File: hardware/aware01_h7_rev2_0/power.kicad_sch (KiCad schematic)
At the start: 23 parts, among them J3 Conn_02x05_Odd_Even, U7 LM1117MP-3.3, U8 LM4040DIM3X-10

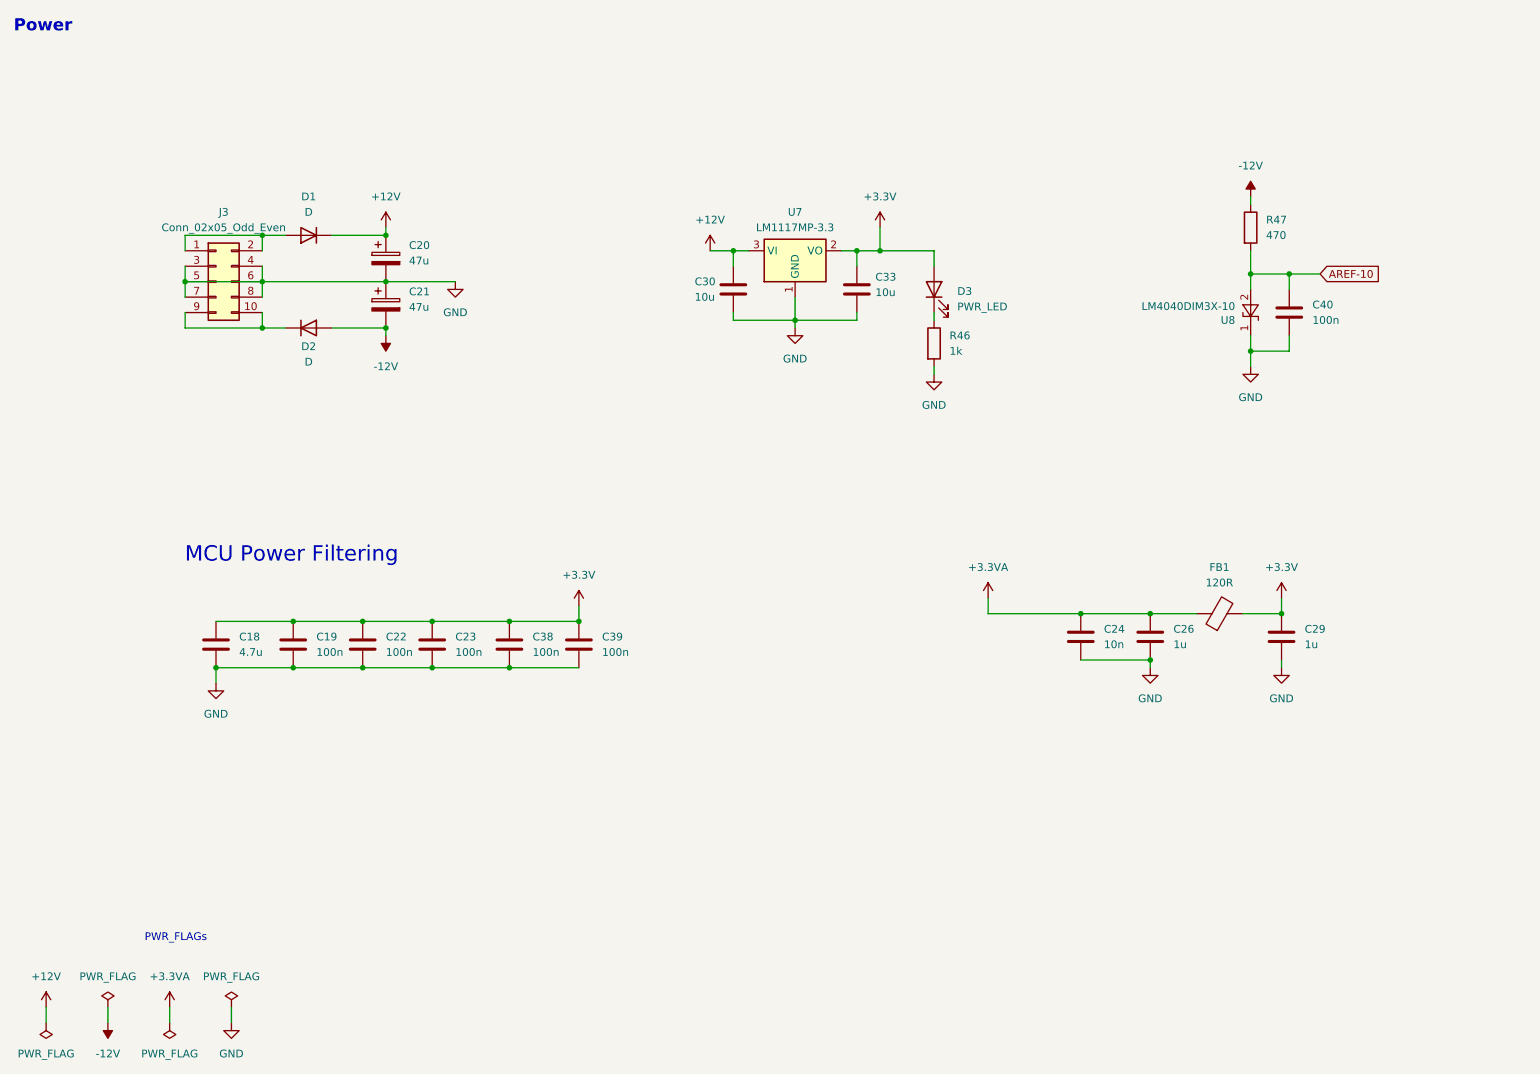
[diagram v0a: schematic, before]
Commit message: add 5V buck converter
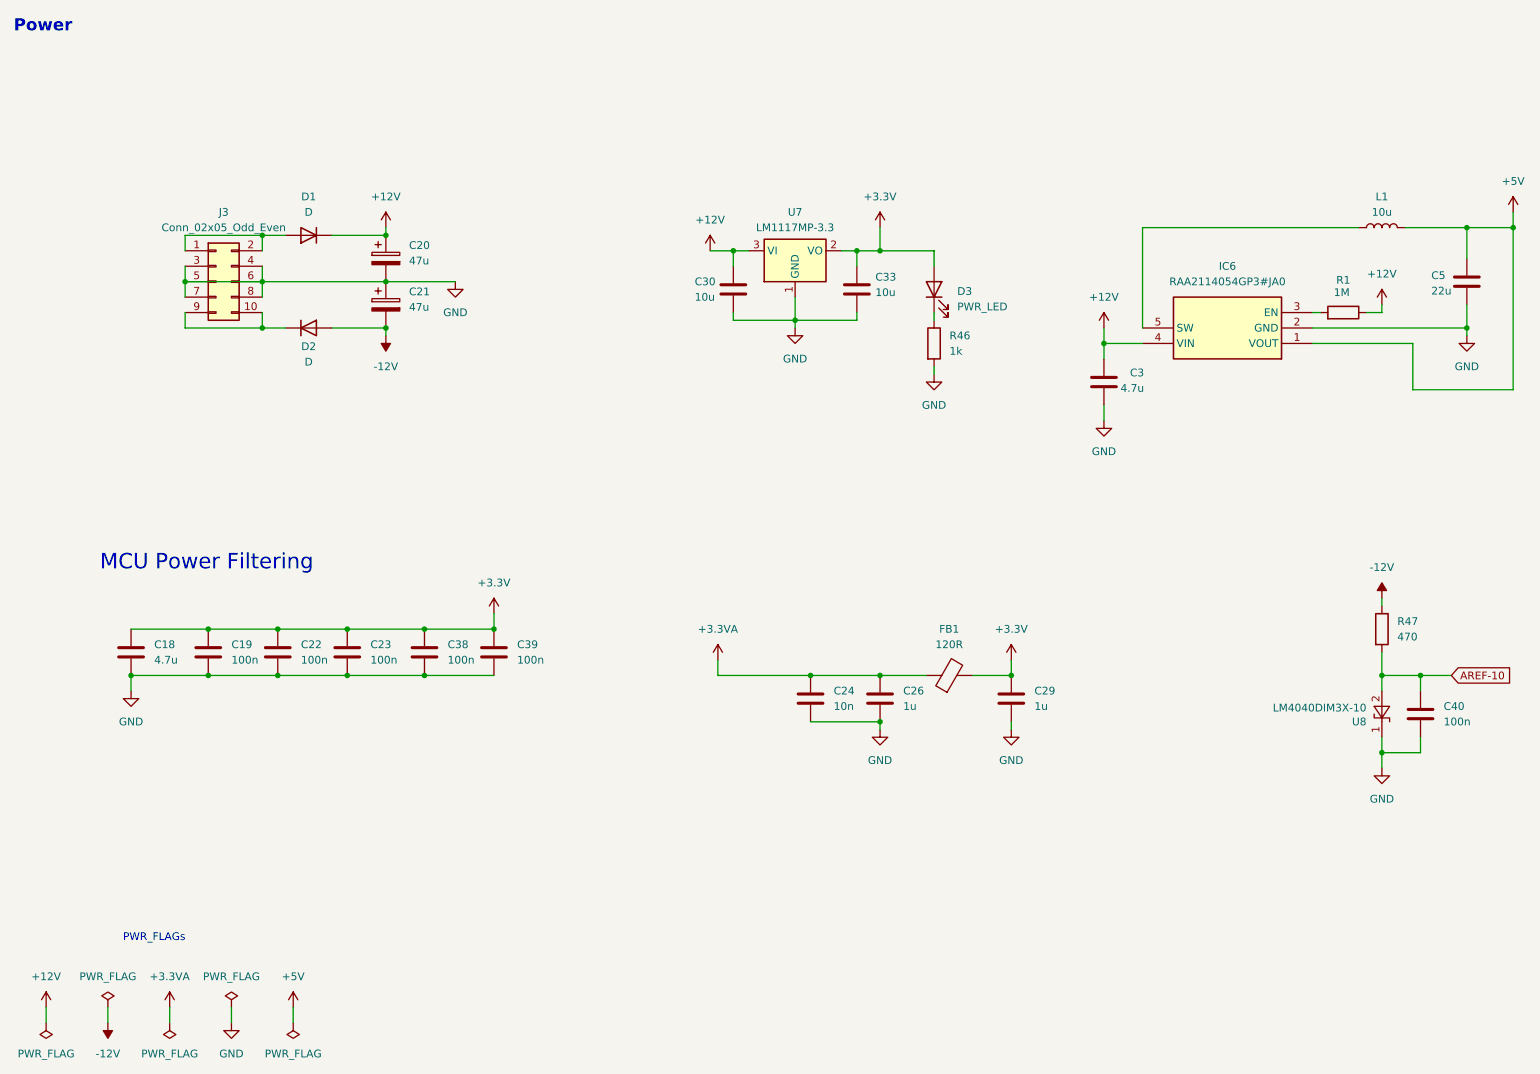
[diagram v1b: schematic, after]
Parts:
- added C3: 4.7u, Capacitor_SMD:C_0603_1608Metric, symbol Device:C
- added C5: 22u, Capacitor_SMD:C_0805_2012Metric_Pad1.18x1.45mm_HandSolder, symbol Device:C
- added IC6: RAA2114054GP3#JA0, Eurorack:RAA2114054GP3#JA0, symbol eurorack_components:RAA2114054GP3#JA0
- added L1: 10u, Eurorack:74438335100, symbol Device:L
- added R1: 1M, Resistor_SMD:R_0603_1608Metric_Pad0.98x0.95mm_HandSolder, symbol Device:R
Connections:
- net +12V: now also C3.2, IC6.4 (VIN), R1.1
- net GND: now also C3.1, C5.2, IC6.2 (GND)
- new net: IC6.3 (EN), R1.2
- new net: IC6.5 (SW), L1.1
- new net +5V: C5.1, IC6.1 (VOUT), L1.2
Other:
- moved on the sheet: C18, C19, C22, C23, C24, C26, C29, C38, C39, C40, FB1, R47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

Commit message: schematic formatting
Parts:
- R1: Manufacturer_Name (none) -> YAGEO; Manufacturer_Part_Number (none) -> RC0603FR-071MP; Mouser Part Number (none) -> 603-RC0603FR-071MP
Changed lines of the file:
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@@
+			)
+		)
+		(property "Manufacturer_Name" " YAGEO"
+			(at 236.22 66.04 90)
+			(effects
+				(font
+					(size 1.27 1.27)
+				)
+				(hide yes)
+			)
+		)
+		(property "Manufacturer_Part_Number" " RC0603FR-071MP"
+			(at 236.22 66.04 90)
+			(effects
+				(font
+					(size 1.27 1.27)
+				)
+				(hide yes)
+			)
+		)
+		(property "Mouser Part Number" " 603-RC0603FR-071MP"
+			(at 236.22 66.04 90)
+			(effects
+				(font
+					(size 1.27 1.27)
+				)
+				(hide yes)
 			)
 		)
